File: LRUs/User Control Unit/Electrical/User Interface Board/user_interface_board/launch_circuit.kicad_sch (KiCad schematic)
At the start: 0 parts

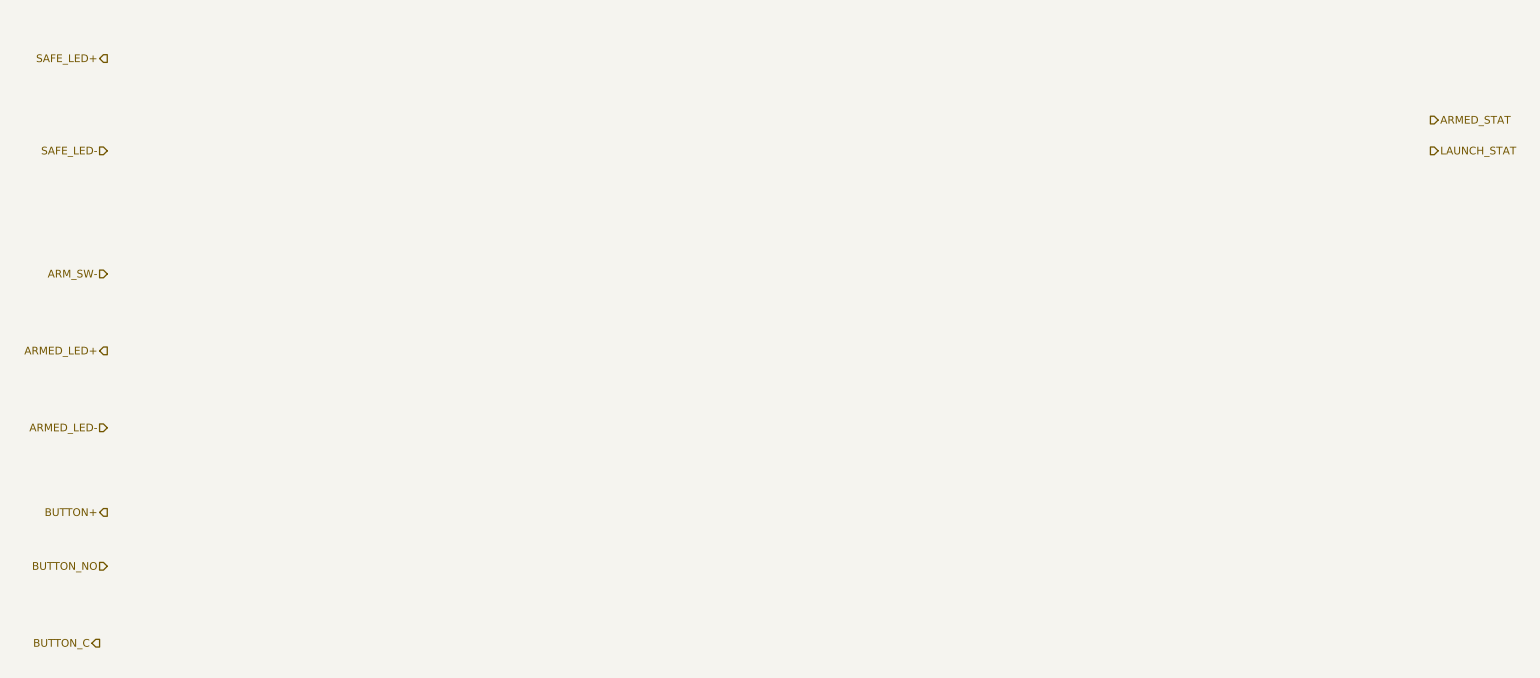
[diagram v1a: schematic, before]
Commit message: interface board schematic
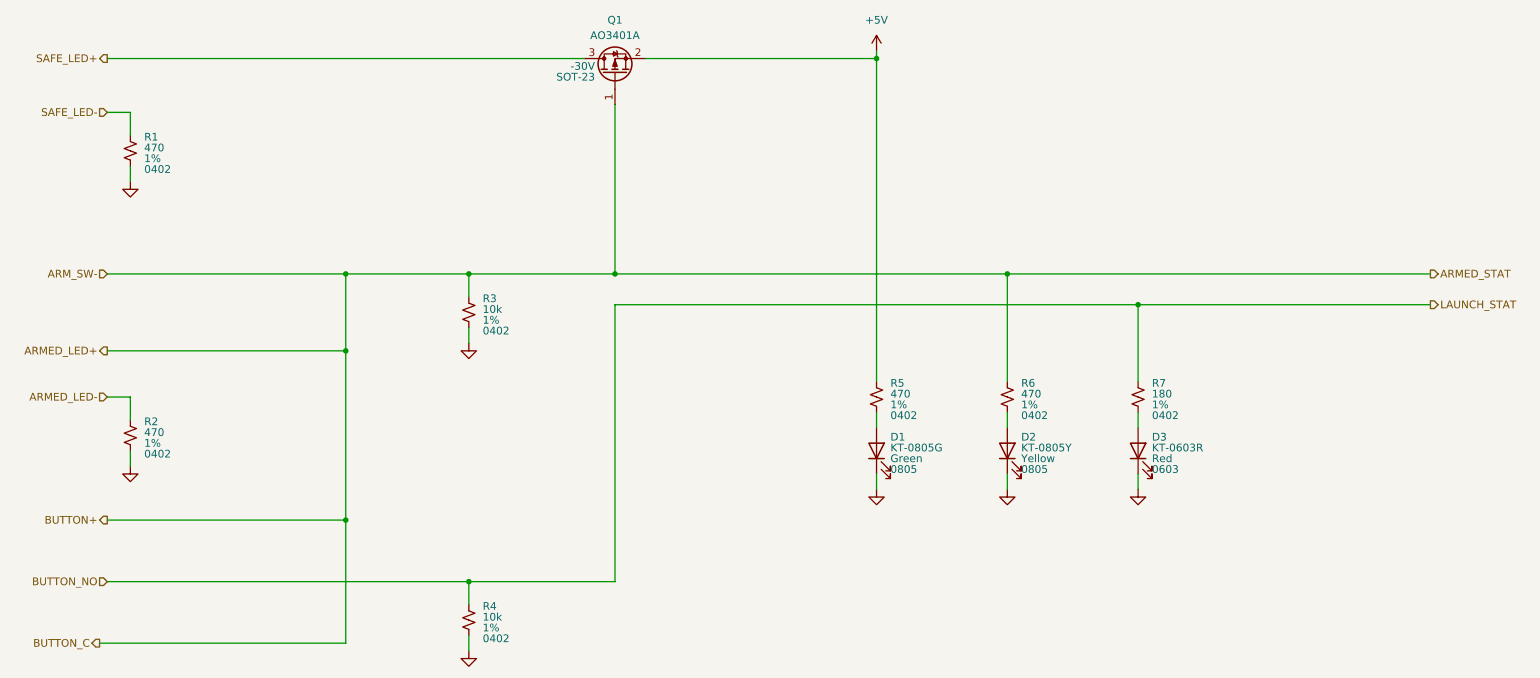
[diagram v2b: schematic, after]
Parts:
- added D1: KT-0805G, LED_SMD:LED_0805_2012Metric, symbol Device:LED
- added D2: KT-0805Y, LED_SMD:LED_0805_2012Metric, symbol Device:LED
- added D3: KT-0603R, LED_SMD:LED_0603_1608Metric, symbol Device:LED
- added Q1: AO3401A, Package_TO_SOT_SMD:SOT-23, symbol Transistor_FET:AO3401A
- added R1, R2, R5, R6: 470, Resistor_SMD:R_0402_1005Metric, symbol Device:R_Small_US
- added R3, R4: 10k, Resistor_SMD:R_0402_1005Metric, symbol Device:R_Small_US
- added R7: 180, Resistor_SMD:R_0402_1005Metric, symbol Device:R_Small_US
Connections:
- net ARMED_LED+: now also Q1.1 (G), R3.1, R6.1
- net ARMED_LED-: now also R2.1
- net BUTTON_NO: now also R4.1, R7.1
- net SAFE_LED+: now also Q1.3 (D)
- net SAFE_LED-: now also R1.1
- new net: D3.2 (A), R7.2
- new net: D2.2 (A), R6.2
- new net: D1.2 (A), R5.2
- new net +5V: Q1.2 (S), R5.1
- new net GND: D1.1 (K), D2.1 (K), D3.1 (K), R1.2, R2.2, R3.2, R4.2

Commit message: fix drc & add level shifter
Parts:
- added R14, R16: 1k, Resistor_SMD:R_0402_1005Metric, symbol Device:R_Small_US
- added R15, R17: 2k, Resistor_SMD:R_0402_1005Metric, symbol Device:R_Small_US
- R3, R4: JLCPCB Part # C17414 -> C25744
- R7: value 180 -> 200; JLCPCB Part # C25117 -> C25087
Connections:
- net ARMED_LED+: now also R14.1
- net BUTTON_NO: now also R16.1
- net GND: now also R15.2, R17.2
- new net ARMED_STAT: R14.2, R15.1
- new net LAUNCH_STAT: R16.2, R17.1

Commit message: style & add prod files
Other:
- title: (none) -> Launch Circuit
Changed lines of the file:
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@@
 	(generator_version "10.0")
 	(paper "A4")
+	(title_block
+		(title "Launch Circuit")
+		(date "2026-10-26")
+		(rev "A")
+	)
 	(junction
 		(at 91.44 60.96)
